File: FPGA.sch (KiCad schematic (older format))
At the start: 10 parts, among them U13 ADS1015, U14 SiT8008B, U8 GW1N-9LQ100

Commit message: Update FPGA.sch
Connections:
- net labels added: PB_MUTE_FPGA
- net labels removed: PB_MUTE
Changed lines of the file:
@@
 Text GLabel 5550 7350 0    50   Output ~ 0
 Motor_off
-Text GLabel 7450 5050 0    50   Input ~ 0
-PB_MUTE
 Text GLabel 7450 5150 0    50   Input ~ 0
 PB_PLUS
@@
 Wire Wire Line
 	6300 6350 6400 6350
+Text GLabel 7450 5050 0    50   Input ~ 0
+PB_MUTE_FPGA
 $EndSCHEMATC

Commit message: Update FPGA.sch
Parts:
- added R? (x2): 33R_Chip_Resistor,_1%,_0.1W, symbol OpenVent:33R_Chip_Resistor,_1%,_0.1W
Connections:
- wire segments 104 -> 106
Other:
- moved on the sheet: U8D
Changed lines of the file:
@@
 Text GLabel 5650 6625 0    50   Output ~ 0
 nPRESSURE-PATIENT-ALERT
-Text GLabel 7450 5750 0    50   Output ~ 0
+Text GLabel 8200 5750 0    50   Output ~ 0
 Sounder_DRV
 $Comp
@@
 Text GLabel 5550 7350 0    50   Output ~ 0
 Motor_off
-Text GLabel 7450 5150 0    50   Input ~ 0
+Text GLabel 8200 5150 0    50   Input ~ 0
 PB_PLUS
-Text GLabel 7450 5250 0    50   Input ~ 0
+Text GLabel 8200 5250 0    50   Input ~ 0
 PB_MINUS
-Text GLabel 7450 5350 0    50   Input ~ 0
+Text GLabel 8200 5350 0    50   Input ~ 0
 PB_SEL
 Text GLabel 9700 1200 2    50   Output ~ 0
@@
 Text GLabel 4450 4400 2    50   Input ~ 0
 Vcap_F
-Text GLabel 9550 5250 2    50   Output ~ 0
+Text GLabel 10300 5250 2    50   Output ~ 0
 LCD_RS
-Text GLabel 9550 5150 2    50   BiDi ~ 0
+Text GLabel 10300 5150 2    50   BiDi ~ 0
 LCD_RW
-Text GLabel 9550 5050 2    50   Output ~ 0
+Text GLabel 10300 5050 2    50   Output ~ 0
 LCD_A_ENABLE
-Text GLabel 9550 4950 2    50   BiDi ~ 0
+Text GLabel 10300 4950 2    50   BiDi ~ 0
 LCD_DB0
-Text GLabel 9550 4850 2    50   BiDi ~ 0
+Text GLabel 10300 4850 2    50   BiDi ~ 0
 LCD_DB1
-Text GLabel 9550 5450 2    50   BiDi ~ 0
+Text GLabel 10300 5450 2    50   BiDi ~ 0
 LCD_DB3
-Text GLabel 9550 5350 2    50   BiDi ~ 0
+Text GLabel 10300 5350 2    50   BiDi ~ 0
 LCD_DB2
-Text GLabel 9550 5650 2    50   BiDi ~ 0
+Text GLabel 10300 5650 2    50   BiDi ~ 0
 LCD_DB5
-Text GLabel 9550 5550 2    50   BiDi ~ 0
+Text GLabel 10300 5550 2    50   BiDi ~ 0
 LCD_DB4
-Text GLabel 9550 5850 2    50   BiDi ~ 0
+Text GLabel 10300 5850 2    50   BiDi ~ 0
 LCD_DB7
-Text GLabel 9550 5750 2    50   BiDi ~ 0
+Text GLabel 10300 5750 2    50   BiDi ~ 0
 LCD_DB6
 Wire Notes Line
@@
 $EndComp
 Wire Wire Line
-	9550 4850 9300 4850
-Wire Wire Line
-	9300 4950 9550 4950
-Wire Wire Line
-	9550 5050 9300 5050
-Wire Wire Line
-	9300 5150 9550 5150
-Wire Wire Line
-	9550 5250 9300 5250
-Wire Wire Line
-	9300 5350 9550 5350
-Wire Wire Line
-	9550 5450 9300 5450
-Wire Wire Line
-	9300 5550 9550 5550
-Wire Wire Line
-	9550 5650 9300 5650
-Wire Wire Line
-	9300 5750 9550 5750
-Wire Wire Line
-	9550 5850 9300 5850
-Wire Wire Line
-	7650 5750 7450 5750
-Wire Wire Line
-	7450 5650 7650 5650
+	10300 4850 10050 4850
+Wire Wire Line
+	10050 4950 10300 4950
+Wire Wire Line
+	10300 5050 10050 5050
+Wire Wire Line
+	10050 5150 10300 5150
+Wire Wire Line
+	10300 5250 10050 5250
+Wire Wire Line
+	10050 5350 10300 5350
+Wire Wire Line
+	10300 5450 10050 5450
+Wire Wire Line
+	10050 5550 10300 5550
+Wire Wire Line
+	10300 5650 10050 5650
+Wire Wire Line
+	10050 5750 10300 5750
+Wire Wire Line
+	10300 5850 10050 5850
+Wire Wire Line
+	8400 5750 8200 5750
+Wire Wire Line
+	8200 5650 8400 5650
 $Comp
 L OpenVent:100nF_0603_Ceramic_Capacitor,_10%,_X7R,_25V C23
@@
 Wire Wire Line
 	7000 2700 6650 2700
-Text GLabel 7450 4950 0    50   Output ~ 0
+Text GLabel 8200 4950 0    50   Output ~ 0
 LCD_B_ENABLE
 Wire Wire Line
-	7650 4950 7450 4950
+	8400 4950 8200 4950
 Wire Notes Line
 	500  2750 5250 2750
@@
 L OpenVent:GW1N-9LQ100 U8
 U 4 1 60544613
-P 8500 4750
-F 0 "U8" H 8475 4998 50  0000 C CNN
-F 1 "GW1N-9LQ100" H 8475 4907 50  0000 C CNN
-F 2 "" H 11800 3850 50  0001 C CNN
-F 3 "" H 11800 3850 50  0001 C CNN
-	4    8500 4750
+P 9250 4750
+F 0 "U8" H 9225 4998 50  0000 C CNN
+F 1 "GW1N-9LQ100" H 9225 4907 50  0000 C CNN
+F 2 "" H 12550 3850 50  0001 C CNN
+F 3 "" H 12550 3850 50  0001 C CNN
+	4    9250 4750
 	1    0    0    -1
 $EndComp
@@
 VBATT-SCALED
 Wire Wire Line
-	7450 5050 7650 5050
-Wire Wire Line
-	7450 5150 7650 5150
-Wire Wire Line
-	7450 5250 7650 5250
-Wire Wire Line
-	7450 5350 7650 5350
+	8200 5050 8400 5050
+Wire Wire Line
+	8200 5150 8400 5150
+Wire Wire Line
+	8200 5250 8400 5250
+Wire Wire Line
+	8200 5350 8400 5350
 Text Notes 5500 650  0    50   ~ 0
 I/Os ON BANKS 0, 2 AND 3 CAN BE FREELY INTERCHANGED AT LAYOUT EXCEPT CLCK WHICH MUST BE ON A GCLKT_x I/O PIN
@@
 	1    0    0    -1
 $EndComp
-Text Label 6550 5550 0    50   ~ 0
+Text Label 7300 5550 0    50   ~ 0
 UART_TX
-Text Label 6550 5450 0    50   ~ 0
+Text Label 7300 5450 0    50   ~ 0
 UART_RX
 $Comp
@@
 Text Notes 5425 5700 1    50   ~ 0
 Debug UART
-Text GLabel 7450 5650 0    50   Output ~ 0
+Text GLabel 8200 5650 0    50   Output ~ 0
 LED_SERIAL_DRV
 Wire Wire Line
@@
 Wire Wire Line
 	6400 5750 6400 5550
-Connection ~ 6400 5550
-Wire Wire Line
-	6400 5550 7650 5550
 Wire Wire Line
 	6150 5750 6150 5450
-Connection ~ 6150 5450
-Wire Wire Line
-	6150 5450 7650 5450
 Wire Wire Line
 	6150 6350 6300 6350
@@
 Wire Wire Line
 	6300 6350 6400 6350
-Text GLabel 7450 5050 0    50   Input ~ 0
+Text GLabel 8200 5050 0    50   Input ~ 0
 PB_MUTE_FPGA
+$Comp
+L OpenVent:33R_Chip_Resistor,_1%,_0.1W R?
+U 1 1 60586513
+P 6750 5650
+F 0 "R?" H 6850 5757 50  0000 C CNN
+F 1 "33R_Chip_Resistor,_1%,_0.1W" H 6400 6000 50  0001 C CNN
+F 2 "" H 6950 5650 50  0001 C CNN
+F 3 "" H 6750 5650 50  0001 C CNN
+F 4 "33R" H 6850 5666 50  0000 C CNN "Val"
+F 5 "1%" H 7300 5650 50  0001 C CNN "Tolerance"
+F 6 "0.1W" H 6750 5650 50  0001 C CNN "Watt"
+	1    6750 5650
+	-1   0    0    1
+$EndComp
+$Comp
+L OpenVent:33R_Chip_Resistor,_1%,_0.1W R?
+U 1 1 6058651C
+P 6750 5550
+F 0 "R?" H 6850 5275 50  0000 C CNN
+F 1 "33R_Chip_Resistor,_1%,_0.1W" H 6400 5900 50  0001 C CNN
+F 2 "" H 6950 5550 50  0001 C CNN
+F 3 "" H 6750 5550 50  0001 C CNN
+F 4 "33R" H 6850 5350 50  0000 C CNN "Val"
+F 5 "1%" H 7300 5550 50  0001 C CNN "Tolerance"
+F 6 "0.1W" H 6750 5550 50  0001 C CNN "Watt"
+	1    6750 5550
+	-1   0    0    1
+$EndComp
+Wire Wire Line
+	6850 5450 8400 5450
+Wire Wire Line
+	6850 5550 8400 5550
+Wire Wire Line
+	6450 5550 6400 5550
+Connection ~ 6400 5550
+Wire Wire Line
+	6450 5450 6150 5450
+Connection ~ 6150 5450
 $EndSCHEMATC

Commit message: Removed attenuation from analogue sensor signals. Removed old ADC U13. Renamed sensor signal names on ADC sheet
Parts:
- removed U13: ADS1015, F_ICs:LT_MS8E, symbol OpenVent:ADS1015
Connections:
- net labels added: FB_DRV_FLOW-SENSOR, FB_DRV_FLOW-SENSOR-GAIN, FB_DRV_OXYGEN-SENSOR, FB_DRV_PRESSURE-SENSOR-PATIENT, FB_DRV_PRESSURE-SENSOR-VENT, Vcap_FLOW-SENSOR, Vcap_FLOW-SENSOR-GAIN, Vcap_OXYGEN-SENSOR, Vcap_PRESSURE-SENSOR-PATIENT, Vcap_PRESSURE-SENSOR-VENT
- net labels removed: FBA_DRV, FBB_DRV, FBC_DRV, FBD_DRV, FBG_DRV, PRESSURE-PATIENT-SENSOR, VBATT-SCALED, Vcap_A, Vcap_B, Vcap_C, Vcap_D, Vcap_G
- wire segments 106 -> 94
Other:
- note removed: "Should this circuit still exist? LM 17/03/21"
- moved on the sheet: R19, R20, U8E, U8F

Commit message: Update FPGA.sch
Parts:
- added Q? (x2): 2N7002BK, symbol OpenVent:2N7002BK
- added R? (x2): 0R0_0603_Chip_Resistor,_1%,_0.1W, symbol OpenVent:0R0_0603_Chip_Resistor,_1%,_0.1W
- added U?: GW1N-9LQ100, symbol OpenVent:GW1N-9LQ100
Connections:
- net Vcap_FLOW-SENSOR is gone; now on net LED_SERIAL_DRV: U8.61 (IOR14A/SO/D1)
- net Vcap_OXYGEN-SENSOR is gone; now on net LCD_RW: U8.73 (RPLL_T_IN/IOR5A)
- net Vcap_PRESSURE-SENSOR-PATIENT is gone; now on net PB_SEL: U8.64 (IOR13A/FASTRD_N/D3)
- net Vcap_PRESSURE-SENSOR-VENT is gone; now on net PB_PLUS: U8.66 (IOR12A/MCS_N/D5)
- net +3V3: now also R?.2, U?.21 (VCCX), U?.26 (VCCO2), U?.38 (VCCO2), U?.54 (VCCX), U?.63 (VCCO1), U?.71 (VCCO1)
- net AD_VREF: now also U8.10 (IOL12A/SCLK), U8.17 (IOL15A/GCLKT_6), U8.19 (IOL20A), U8.6 (IOL9A/GCLKT_7), U8.92 (IOT17B), U8.94 (IOT15B), U8.98 (IOT8B); no longer U8.56 (GCLKC_3/IOR17B), U8.58 (DOUT/WE_N/IOR15B), U8.60 (IOR14B/SSPI_CS_N/D0), U8.62 (IOR13B/SI/D2), U8.65 (IOR12B/MCLK/D4), U8.69 (GCLKC_2/IOR9B), U8.72 (RPLL_C_IN/IOR5B)
- net GND: now also Q?.2 (S), Q?.2 (S), U?.2 (GND), U?.24 (GND), U?.37 (GND), U?.52 (GND), U?.74 (GND), U?.87 (GND)
- net LCD_A_ENABLE: now also U8.59 (DIN/CLKHOLD_N/IOR15A); no longer U8.90 (IOT22A)
- net LCD_B_ENABLE: now also U8.58 (DOUT/WE_N/IOR15B); no longer U8.19 (IOL20A)
- net LCD_DB0: now also U8.70 (GCLKT_2/IOR9A); no longer U8.85 (IOT32B)
- net LCD_DB1: now also U8.69 (GCLKC_2/IOR9B); no longer U8.86 (IOT32A)
- net LCD_DB2: now also U8.57 (GCLKT_3/IOR17A); no longer U8.92 (IOT17B)
- net LCD_DB3: now also U8.56 (GCLKC_3/IOR17B); no longer U8.95 (IOT15A)
- net LCD_DB4: now also U8.80 (IOT41A); no longer U8.94 (IOT15B)
- net LCD_DB5: now also U8.79 (IOT41B); no longer U8.97 (IOT12A)
- net LCD_DB6: now also U8.78 (IOT42A); no longer U8.96 (IOT12B)
- net LCD_DB7: now also U8.77 (IOT42B); no longer U8.91 (IOT20A)
- net LCD_RS: now also U8.72 (RPLL_C_IN/IOR5B); no longer U8.93 (IOT17A)
- net LCD_RW: no longer U8.89 (IOT22B)
- net LED_SERIAL_DRV: no longer U8.99 (IOT8A)
- net PB_MINUS: now also U8.65 (IOR12B/MCLK/D4); no longer U8.18 (IOL15B/GCLKC_6)
- net PB_MUTE_FPGA: now also U8.67 (IOR11B/MO/D6); no longer U8.20 (IOL20B)
- net PB_PLUS: no longer U8.17 (IOL15A/GCLKT_6)
- net PB_SEL: no longer U8.6 (IOL9A/GCLKT_7)
- net Sounder_DRV: now also U8.60 (IOR14B/SSPI_CS_N/D0); no longer U8.98 (IOT8B)
- net UART_RX: now also U8.82 (IOT39A); no longer U8.7 (IOL9B/GCLKC_7)
- net UART_TX: now also U8.81 (IOT39B); no longer U8.10 (IOL12A/SCLK)
- net Vcap_E: now also U8.95 (IOT15A); no longer U8.70 (GCLKT_2/IOR9A)
- net Vcap_F: now also U8.97 (IOT12A); no longer U8.57 (GCLKT_3/IOR17A)
- net Vcap_FLOW-SENSOR-GAIN: no longer U8.59 (DIN/CLKHOLD_N/IOR15A)
- net Motor_Off: now reaches U8.41 (IOB29A/GCLKT_4)
- net Motor_Off: now also Q?.1 (G1), Q?.1 (G1)
- new net: R?.1, R?.1, U?.1 (VCC), U?.25 (VCC), U?.51 (VCC), U?.75 (VCC)
- new net +3.3V: U?.13 (VCCO3), U?.4 (VCCO3), U?.76 (VCCO0), U?.88 (VCCO0)
- new net +5V: R?.2
- new net Vcap_FLOW_SEN: U8.99 (IOT8A)
- new net Vcap_OXY: U8.20 (IOL20B)
- new net Vcap_PRES-SENS-PAT: U8.7 (IOL9B/GCLKC_7)
- new net Vcap_PRES-SENS-VENT: U8.18 (IOL15B/GCLKC_6)
- new net nMOTOR-FAULT-A: Q?.3 (D)
- new net nMOTOR-FAULT-B: Q?.3 (D)
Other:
- note added: "DO NOT FIT"
- note added: "I/Os ON BANKS 1 AND 2 CAN BE FREELY INTERCHANGED AT LAYOUT EXCEPT CLCK WHICH MUST BE ON A GCLKT_x I/O PIN"
- note removed: "Bank 1 = +3V3_Sensors if GOW1N -9 or 3V3 if GOWIN -4"
- note removed: "I/Os ON BANKS 0, 2 AND 3 CAN BE FREELY INTERCHANGED AT LAYOUT EXCEPT CLCK WHICH MUST BE ON A GCLKT_x I/O PIN"
- moved on the sheet: C23, JP5, R19, R20, R41, R?, TVS-D3, TVS-D4, U14, U8D, U8E, U8F

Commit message: Update FPGA.sch
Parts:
- U8, U?: symbol OpenVent:GW1N-9LQ100 -> OpenVent-rescue:GW1N-9LQ100-OpenVent
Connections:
- net AD_VREF: now also U8.86 (IOT32A), U8.90 (IOT22A), U8.97 (IOT12A), U8.99 (IOT8A); no longer U8.10 (IOL12A/SCLK), U8.92 (IOT17B), U8.94 (IOT15B), U8.98 (IOT8B)
- net Vcap_E: now also U8.89 (IOT22B); no longer U8.95 (IOT15A)
- net Vcap_F: now also U8.85 (IOT32B); no longer U8.97 (IOT12A)
- net Vcap_FLOW-SENSOR-GAIN: now also U8.96 (IOT12B)
- net Vcap_FLOW_SEN: now also U8.98 (IOT8B); no longer U8.99 (IOT8A)
- net Vcap_OXY: now also U8.7 (IOL9B/GCLKC_7); no longer U8.20 (IOL20B)
- net Vcap_PRES-SENS-PAT: now also U8.20 (IOL20B); no longer U8.7 (IOL9B/GCLKC_7)
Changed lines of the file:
@@
 	7400 2100 7300 2100
 $Comp
-L OpenVent:GW1N-9LQ100 U8
+L OpenVent-rescue:GW1N-9LQ100-OpenVent U8
 U 6 1 6053AF87
 P 8600 4200
@@
 Connection ~ 3900 1600
 $Comp
-L OpenVent:GW1N-9LQ100 U?
+L OpenVent-rescue:GW1N-9LQ100-OpenVent U?
 U 1 1 605DEC3D
 P 3000 1450
 AR Path="/5FBE8499/605DEC3D" Ref="U?"  Part="1"
 AR Path="/5F8F894A/605DEC3D" Ref="U?"  Part="1"
+AR Path="/605DEC3D" Ref="U?"  Part="1"
 F 0 "U?" H 3025 1615 50  0000 C CNN
 F 1 "GW1N-9LQ100" H 3025 1524 50  0000 C CNN
@@
 	6650 2600 7400 2600
 $Comp
-L OpenVent:GW1N-9LQ100 U8
+L OpenVent-rescue:GW1N-9LQ100-OpenVent U8
 U 4 1 60544613
 P 3200 3850
@@
 	7400 2400 7250 2400
 $Comp
-L OpenVent:GW1N-9LQ100 U8
+L OpenVent-rescue:GW1N-9LQ100-OpenVent U8
 U 5 1 6054191D
 P 8200 1300

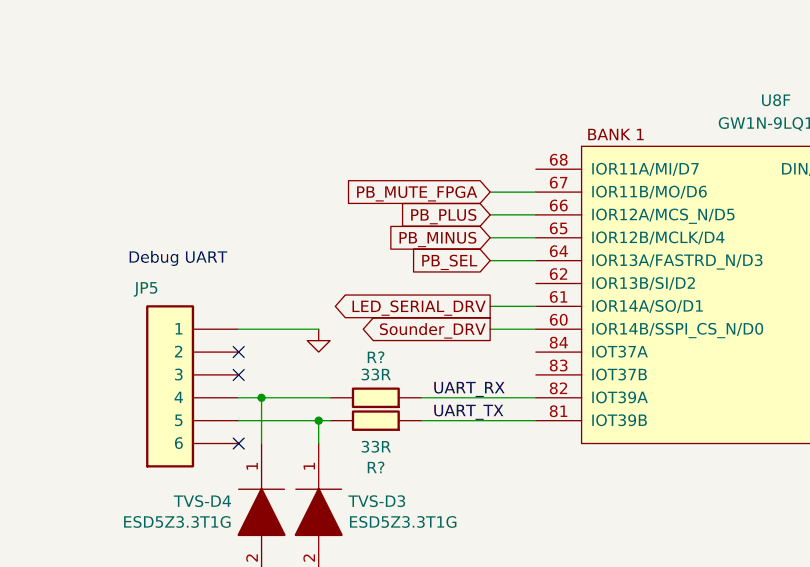
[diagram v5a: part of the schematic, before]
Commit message: Moved SOUNDER-CURRENT input signal from MCU to FPGA
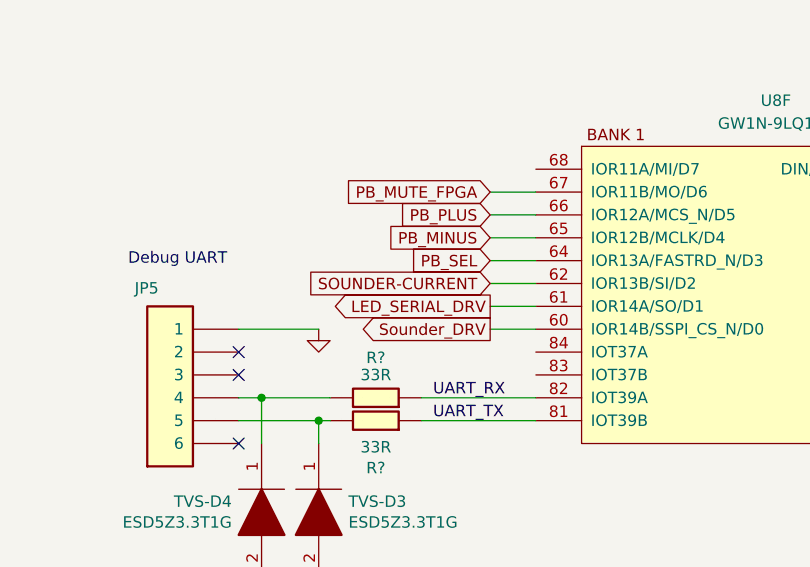
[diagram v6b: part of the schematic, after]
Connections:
- net SOUNDER-CURRENT: now reaches U8.62 (IOR13B/SI/D2)
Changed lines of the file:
@@
 	9050 2500 9950 2500
 Connection ~ 9950 2500
+Text GLabel 7350 4800 0    50   Input ~ 0
+SOUNDER-CURRENT
+Wire Wire Line
+	7550 4800 7350 4800
 $EndSCHEMATC

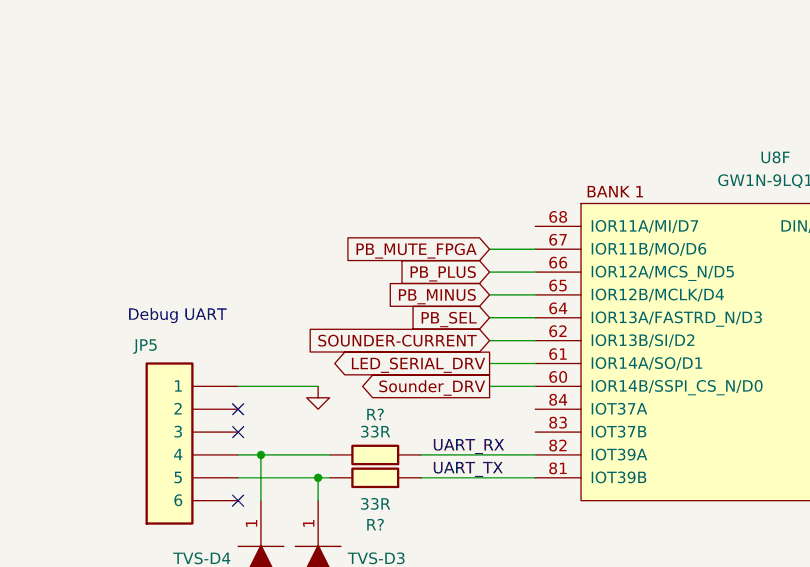
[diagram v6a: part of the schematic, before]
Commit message: Update FPGA.sch
PB_SEL_FPGA added
PB_MUTE_FPGA back to PB_MUTE
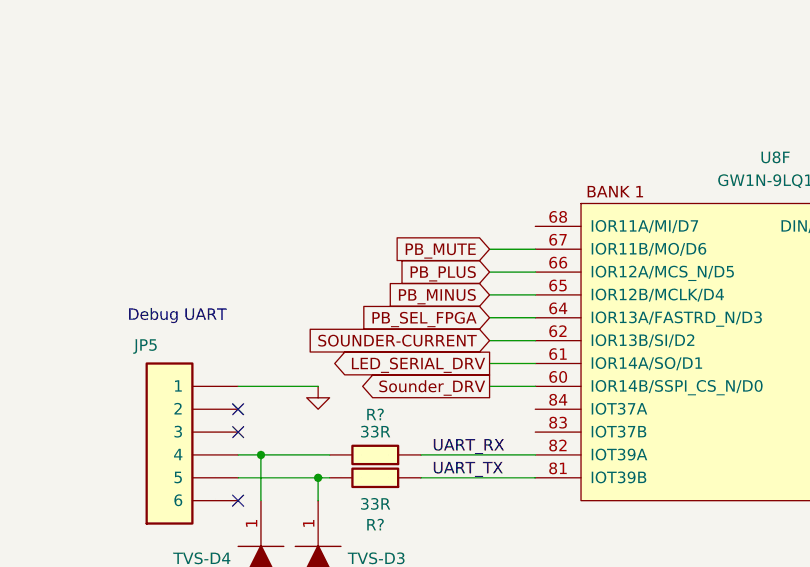
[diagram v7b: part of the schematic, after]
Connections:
- net PB_MUTE_FPGA renamed PB_MUTE
- net PB_SEL renamed PB_SEL_FPGA
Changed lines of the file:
@@
 $Descr A4 11693 8268
 encoding utf-8
-Sheet 6 9
+Sheet 4 9
 Title "OpenVent Control Board"
 Date "2020-10-20"
@@
 PB_MINUS
 Text GLabel 7350 4700 0    50   Input ~ 0
-PB_SEL
+PB_SEL_FPGA
 Text GLabel 9300 1400 2    50   Output ~ 0
 Vref_DRV
@@
 	6500 6100 6600 6100
 Text GLabel 7350 4400 0    50   Input ~ 0
-PB_MUTE_FPGA
+PB_MUTE
 $Comp
 L OpenVent:33R_Chip_Resistor,_1%,_0.1W R?
